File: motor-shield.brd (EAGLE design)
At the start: 65 x 56 mm, 30 parts, among them IC1 24AA01P, K1 PIN20X2

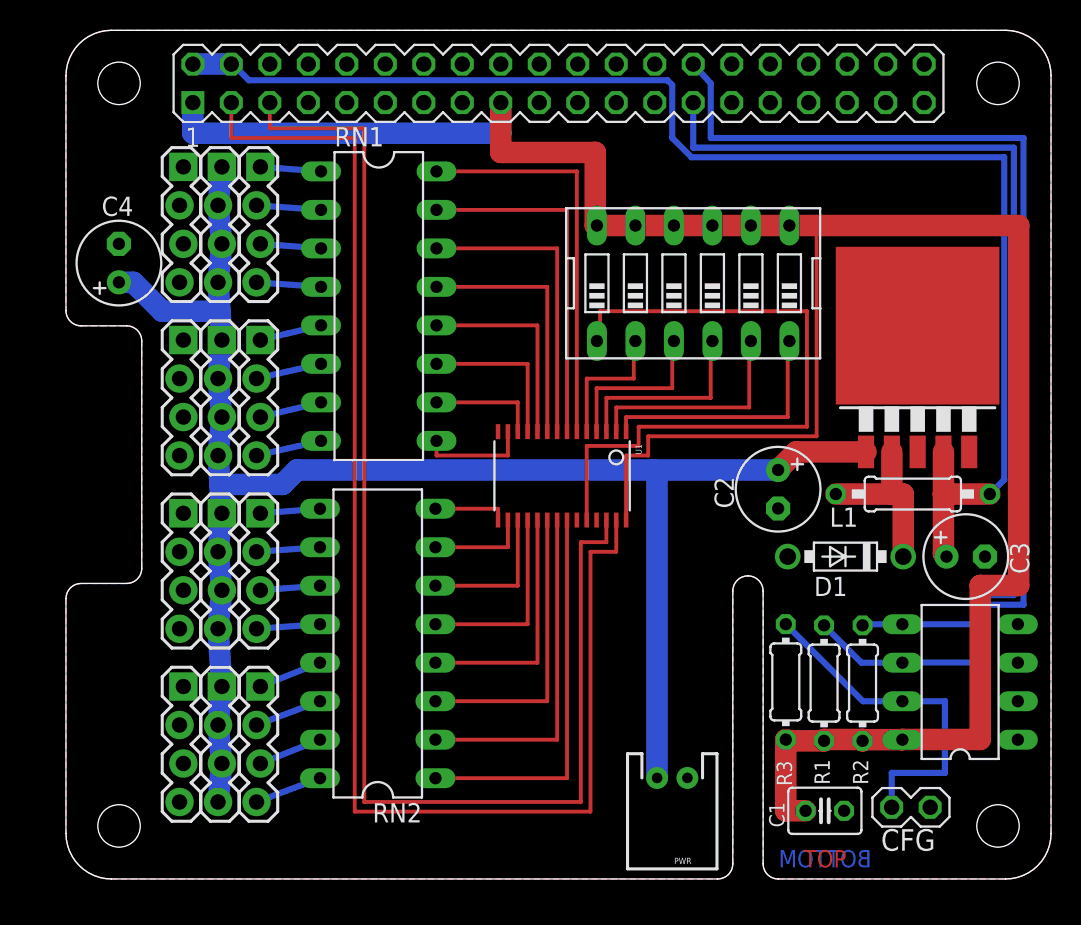
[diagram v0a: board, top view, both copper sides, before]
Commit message: Complete, no air wires, passes DRC
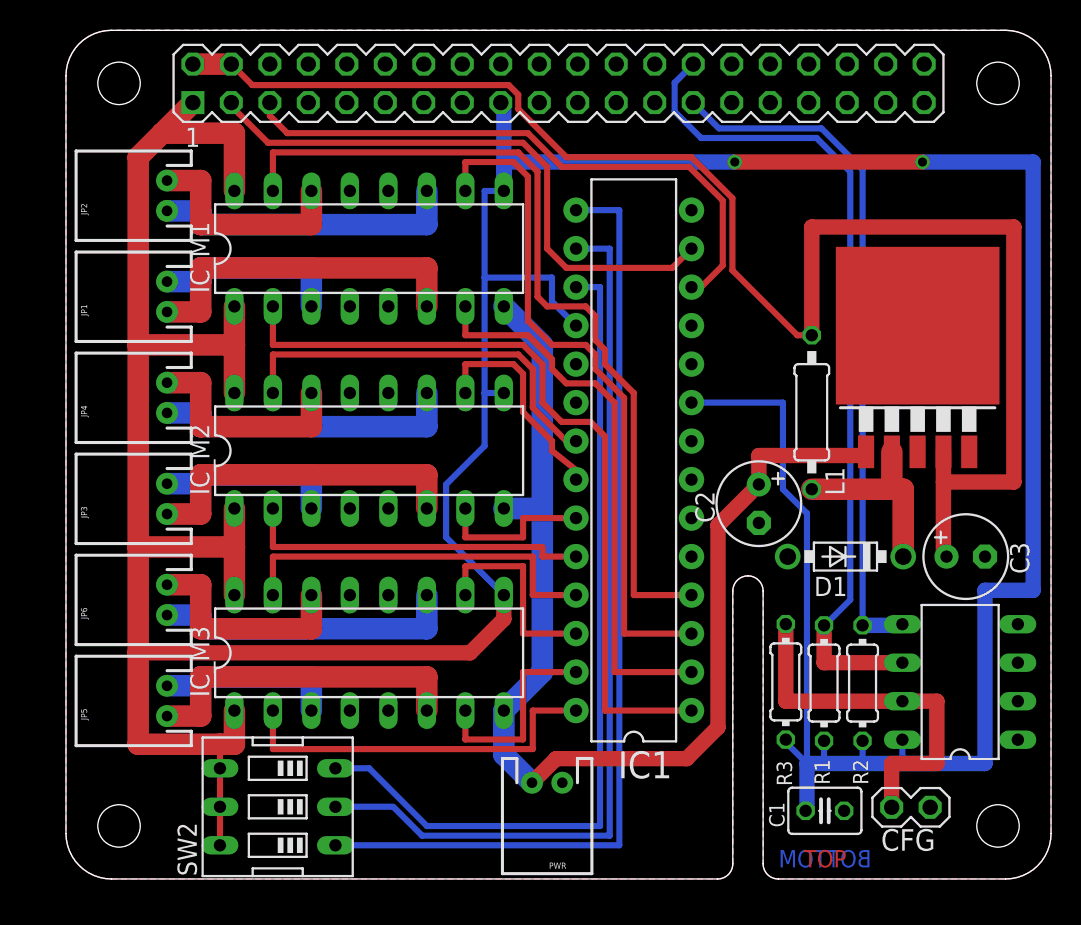
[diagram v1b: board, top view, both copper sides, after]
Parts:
- removed C4: 640uf, rcl:E2,5-6
- removed JP10, JP11, JP12, JP7, JP8, JP9: (no value), SparkFun-Connectors:1X04_LOCK
- removed RN1, RN2: (no value), resistor-dil:DIL16
- removed SW1: (no value), special:EDG-06
- removed U1: (no value), adafruit:TSSOP28
- added IC_ID: 24AA01P, microchip:DIL8
- added IC_M1, IC_M2, IC_M3: L293D, st-microelectronics:DIL16
- added SW2: (no value), special:EDG-03
- IC1: value 24AA01P -> MCP23017SP2; device microchip:DIL8 -> adafruit:DIL28-3-ROUND
- JP1, JP2, JP3, JP4, JP5, JP6: value (none) -> M02JST-PTH-2; device SparkFun-Connectors:1X04_LOCK -> SparkFun-Connectors:JST-2-PTH
- PWR: value (none) -> M02JST-PTH-2
- moved JP5 35.4 mm to (6.67, 11.7), turned to 90 degrees
- moved IC1 26.0 mm to (37.5, 27.6)
- moved JP4 20.0 mm to (6.67, 31.8), turned to 90 degrees
- moved JP6 17.5 mm to (6.67, 18.4), turned to 90 degrees
- moved JP2 11.3 mm to (6.67, 45.1), turned to 90 degrees
- moved JP1 10.5 mm to (6.67, 38.4), turned to 90 degrees
- moved L1 8.58 mm to (49.2, 30.8), turned to 90 degrees
- moved PWR 8.26 mm to (31.8, 6.35)
- moved JP3 6.11 mm to (6.67, 25.1), turned to 90 degrees
- moved C2 1.59 mm to (45.7, 24.8)
- renumbered IC2 to IC_PWR
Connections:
- removed net N$21: JP4.3, RN2.15
- removed net N$22: JP4.4, RN2.16
- removed net N$23: RN2.1, U1.22
- removed net N$24: RN2.2, U1.21
- removed net N$25: RN2.3, U1.20
- removed net N$26: RN2.4, U1.19
- removed net N$27: RN2.5, U1.18
- removed net N$28: RN2.6, U1.17
- removed net N$29: RN1.10, U1.12
- removed net N$30: RN1.11, U1.11
- removed net N$31: RN1.12, U1.10
- removed net N$32: RN1.13, U1.9
- removed net N$33: RN1.14, U1.8
- removed net N$34: RN1.15, U1.7
- removed net N$35: RN1.16, U1.6
- removed net N$36: JP2.1, RN1.5
- removed net N$37: JP2.4, RN1.8
- removed net N$38: JP2.3, RN1.7
- removed net N$39: JP2.2, RN1.6
- new net M1A: IC1.1, IC_M1.2
- new net M1B: IC1.4, IC_M1.15
- new net M2A: IC1.2, IC_M1.7
- new net M2B: IC1.3, IC_M1.10
- new net M3A: IC1.24, IC_M2.2
- new net M3B: IC1.21, IC_M2.15
- new net M4A: IC1.23, IC_M2.7
- new net M4B: IC1.22, IC_M2.10
- new net M5A: IC1.28, IC_M3.2
- new net M5B: IC1.25, IC_M3.15
- new net M6A: IC1.27, IC_M3.7
- new net M6B: IC1.26, IC_M3.10
- net +3V3: now also IC1.18, IC1.9, IC_ID.8, IC_M1.1, IC_M1.16, IC_M1.9, IC_M2.1, IC_M2.16, IC_M2.9, IC_M3.1, IC_M3.16, IC_M3.9, SW2.4, SW2.5, SW2.6; no longer IC1.8, SW1.10, SW1.11, SW1.12, SW1.7, SW1.8, SW1.9, U1.28
- net GND: now also IC1.10, IC_ID.1, IC_ID.2, IC_ID.3, IC_ID.4, IC_M1.12, IC_M1.13, IC_M1.4, IC_M1.5, IC_M2.12, IC_M2.13, IC_M2.4, IC_M2.5, IC_M3.12, IC_M3.13, IC_M3.4, IC_M3.5; no longer C4.-, IC1.1, IC1.2, IC1.3, IC1.4, JP10.1, JP10.2, JP10.3, JP10.4, JP11.1, JP11.2, JP11.3, JP11.4, JP12.1, JP12.2, JP12.3, JP12.4, JP9.1, JP9.2, JP9.3, JP9.4, U1.14, U1.25
- net I2C_SCL: now also IC1.12; no longer U1.26
- net I2C_SDA: now also IC1.13; no longer U1.27
- net ID_SCL: now also IC_ID.6; no longer IC1.6
- net ID_SDA: now also IC_ID.5; no longer IC1.5
- net N$1: now also IC1.17, SW2.3; no longer RN2.7, U1.16
- net N$10: now also IC_M1.3, JP1.2; no longer JP3.2, RN2.10
- net N$11: now also IC_M2.6, JP3.1; no longer SW1.1, U1.24
- net N$12: now also IC_M2.3, JP3.2; no longer SW1.2, U1.5
- net N$13: now also IC_M3.11, JP6.1; no longer SW1.3, U1.4
- net N$14: now also IC_M3.14, JP6.2; no longer SW1.4, U1.3
- net N$15: now also IC_M3.6, JP5.1; no longer SW1.5, U1.2
- net N$16: now also IC_M3.3, JP5.2; no longer SW1.6, U1.1
- net N$17: now also IC1.8; no longer JP3.3, RN2.11
- net N$18: now also IC1.7; no longer JP3.4, RN2.12
- net N$19: now also IC1.6; no longer JP4.1, RN2.13
- net N$2: now also IC1.16, SW2.2; no longer RN2.8, U1.15
- net N$20: now also IC1.5; no longer JP4.2, RN2.14
- net N$3: now also IC1.15, SW2.1; no longer RN1.9, U1.13
- net N$4: now also IC_ID.7; no longer IC1.7
- net N$5: now also IC_M2.11, JP4.1; no longer JP1.4, RN1.4
- net N$6: now also IC_M2.14, JP4.2; no longer JP1.3, RN1.3
- net N$7: now also IC_M1.11, JP2.1; no longer JP1.2, RN1.2
- net N$8: now also IC_M1.14, JP2.2; no longer JP1.1, RN1.1
- net N$9: now also IC_M1.6, JP1.1; no longer JP3.1, RN2.9
- net V+: now also IC_M1.8, IC_M2.8, IC_M3.8; no longer C4.+, JP5.1, JP5.2, JP5.3, JP5.4, JP6.1, JP6.2, JP6.3, JP6.4, JP7.1, JP7.2, JP7.3, JP7.4, JP8.1, JP8.2, JP8.3, JP8.4
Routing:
- net +3V3: track 154.3 -> 296.7 mm, vias 0 -> 2
- net M1B: track 0.00 -> 56.4 mm
- net N$3: track 7.26 -> 63.5 mm
- net N$2: track 4.88 -> 59.8 mm
- net I2C_SDA: track 91.4 -> 38.7 mm
- net M1A: track 0.00 -> 52.2 mm
- net N$1: track 6.57 -> 56.2 mm
- net I2C_SCL: track 87.0 -> 40.0 mm
- net M2B: track 0.00 -> 45.0 mm
- net M2A: track 0.00 -> 36.8 mm
- net V+: track 113.5 -> 77.0 mm
- net N$35: track 26.4 -> 0.00 mm
- net M3B: track 0.00 -> 26.4 mm
- net N$23: track 25.7 -> 0.00 mm
- net M5A: track 0.00 -> 25.1 mm
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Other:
- outline, holes or cut-outs redrawn

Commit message: Rebuilt to match servo shield
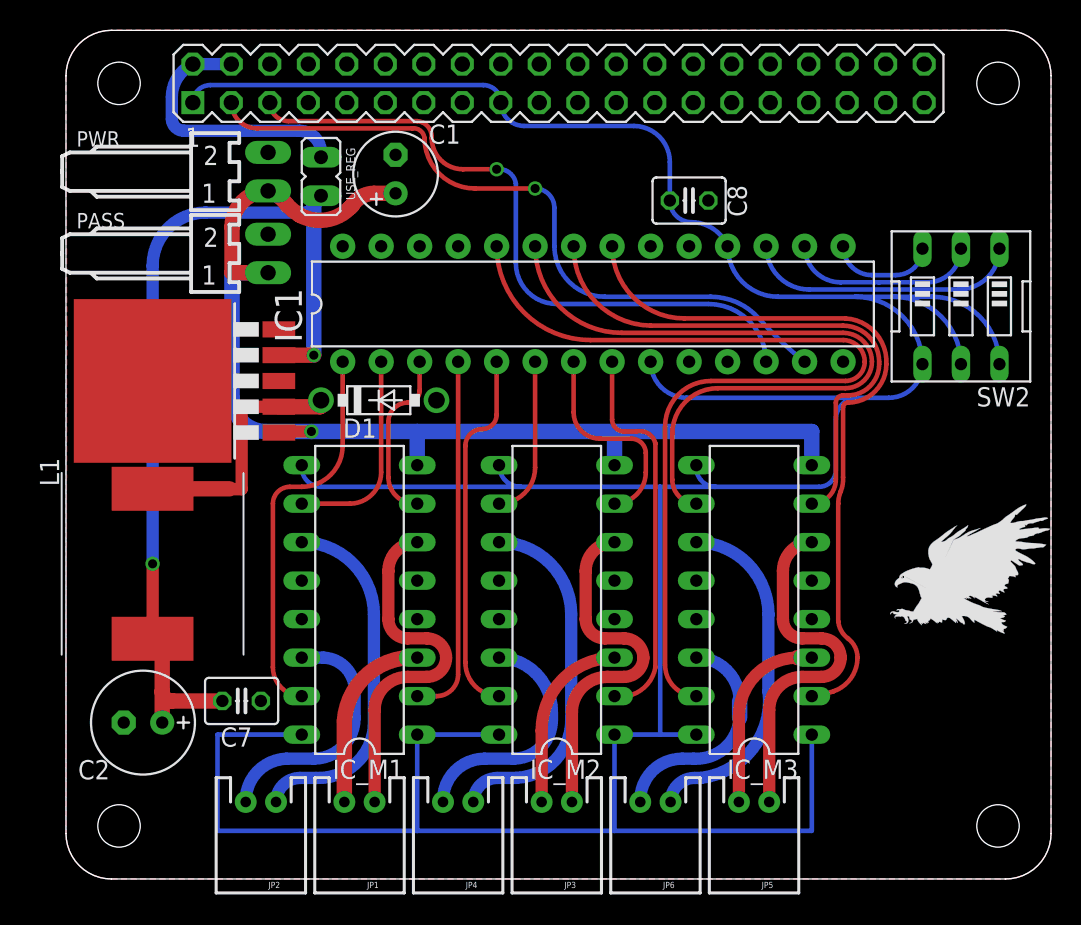
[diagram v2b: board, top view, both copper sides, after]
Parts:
- removed C3: 220uf, rcl:E2,5-6
- removed CFG: (no value), FLYFISH:PIN_W_2
- removed IC_ID: 24AA01P, microchip:DIL8
- removed IC_PWR: (no value), linear:TO263-5
- removed R1, R2: 3k9, rcl:0204/7
- removed R3: 1k, rcl:0204/7
- added C7, C8: 100nf, rcl:C025-030X050
- added IC2: (no value), linear:TO263-5
- added PASS: 22-05-7028-02, con-molex:7395-02
- added U$1: (no value), logo:EAGLE-PLC-8MM
- added USE_REG: (no value), jumper:JP1
- C1: value 100nF -> 1000uf; device rcl:C025-030X050 -> rcl:E2,5-6
- C2: value 680uf -> 1000uf; device rcl:E2,5-6 -> rcl:E2,5-7
- L1: device rcl:0207/10 -> WE-PD:WE-PD_1260/1245/1280/1210
- PWR: value M02JST-PTH-2 -> 22-05-7028-02; device SparkFun-Connectors:JST-2-PTH -> con-molex:7395-02
- moved SW2 55.9 mm to (59.1, 37.8), turned to 180 degrees
- moved C1 50.7 mm to (21.7, 46.5), turned to 90 degrees
- moved L1 44.6 mm to (5.71, 20.8), turned to 270 degrees
- moved PWR 44.3 mm to (13.3, 46.7), turned to 270 degrees
- moved C2 43.1 mm to (5.08, 10.3), turned to 180 degrees
- moved JP2 40.5 mm to (12.9, 5.08), turned to 180 degrees
- moved JP5 39.3 mm to (45.4, 5.08), turned to 180 degrees
- moved JP1 35.7 mm to (19.4, 5.08), turned to 180 degrees
- moved JP6 34.9 mm to (38.9, 5.08), turned to 180 degrees
- moved JP4 32.9 mm to (25.9, 5.08), turned to 180 degrees
- moved JP3 32.6 mm to (32.4, 5.08), turned to 180 degrees
- moved D1 32.5 mm to (20.6, 31.6), turned to 0 degrees
- moved IC_M3 25.6 mm to (45.4, 18.4), turned to 90 degrees
- moved IC_M1 23.2 mm to (19.4, 18.4), turned to 90 degrees
- moved IC_M2 15.8 mm to (32.4, 18.4), turned to 90 degrees
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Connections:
- removed net M1A: IC1.1, IC_M1.2
- removed net M1B: IC1.4, IC_M1.15
- removed net M2A: IC1.2, IC_M1.7
- removed net M2B: IC1.3, IC_M1.10
- removed net M3A: IC1.24, IC_M2.2
- removed net M3B: IC1.21, IC_M2.15
- removed net M4A: IC1.23, IC_M2.7
- removed net M4B: IC1.22, IC_M2.10
- removed net N$1 (its old number): IC1.17, SW2.3
- removed net N$17: IC1.8
- removed net N$18: IC1.7
- removed net N$19: IC1.6
- removed net N$20: IC1.5
- removed net N$3 (its old number): IC1.15, SW2.1
- removed net N$4: CFG.1, IC_ID.7, R3.1
- removed net N$40: D1.C, IC_PWR.2, L1.1
- new net 1F: IC1.4, IC_M1.2
- new net 1R: IC1.3, IC_M1.7
- new net 2F: IC1.1, IC_M1.15
- new net 2R: IC1.2, IC_M1.10
- new net 3F: IC1.8, IC_M2.2
- new net 3R: IC1.7, IC_M2.7
- new net 4F: IC1.5, IC_M2.15
- new net 4R: IC1.6, IC_M2.10
- new net 5F: IC1.21, IC_M3.2
- new net 5R: IC1.22, IC_M3.7
- new net 6F: IC1.24, IC_M3.15
- new net 6R: IC1.23, IC_M3.10
- new net N$16: K1.2, K1.4, USE_REG.2
- new net N$2: IC1.15, SW2.3
- new net N$23: IC1.17, SW2.1
- new net VOUT: D1.C, IC2.2, L1.1
- net +3V3: now also C8.1; no longer C1.1, IC_ID.8, R1.2, R2.2, R3.2
- net +5V: now also C2.+, C7.1, IC2.4, USE_REG.1; no longer C3.+, IC_PWR.4, K1.2, K1.4
- net GND: now also C1.-, C7.2, C8.2, IC2.3, IC2.5, IC2.6, PASS.2, PWR.2; no longer C1.2, C3.-, CFG.2, IC_ID.1, IC_ID.2, IC_ID.3, IC_ID.4, IC_PWR.3, IC_PWR.5, IC_PWR.6, PWR.1
- net ID_SCL: no longer IC_ID.6, R1.1
- net ID_SDA: no longer IC_ID.5, R2.1
- net M5A: no longer IC_M3.2
- net M5B: no longer IC_M3.15
- net M6A: no longer IC_M3.7
- net M6B: no longer IC_M3.10
- net V+: now also C1.+, IC2.1, PASS.1, PWR.1; no longer C2.+, IC_PWR.1, PWR.2
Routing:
- net N$3 (its old number): track 63.5 -> 0.00 mm
- net 6F: track 0.00 -> 61.0 mm
- net +3V3: track 296.7 -> 238.1 mm, vias 2 -> 0
- net M1B: track 56.4 -> 0.00 mm
- net N$1 (its old number): track 56.2 -> 0.00 mm
- net ID_SCL: track 55.2 -> 0.00 mm
- net M1A: track 52.2 -> 0.00 mm
- net N$3: track 59.8 -> 12.2 mm
- net 5F: track 0.00 -> 46.5 mm
- net 6R: track 0.00 -> 45.8 mm
- net ID_SDA: track 45.8 -> 0.00 mm
- net M2B: track 45.0 -> 0.00 mm
- net +5V: track 100.7 -> 60.2 mm, vias 0 -> 2
- net M2A: track 36.8 -> 0.00 mm
- net 5R: track 0.00 -> 34.8 mm
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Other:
- outline, holes or cut-outs redrawn
- board text removed: "BOTTOM"
- board text removed: "TOP"

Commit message: ROTATE THE EAGLE
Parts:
- moved U$1 14.8 mm to (50.5, 3.33), turned to 0 degrees
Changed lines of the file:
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@@
 <attribute name="VALUE" x="10.8951" y="43.2704" size="0.8128" layer="27" ratio="10" rot="R180"/>
 </element>
-<element name="U$1" library="logo" package="EAGLE-PLC-8MM" value="" x="53.6575" y="17.78" rot="R330"/>
+<element name="U$1" library="logo" package="EAGLE-PLC-8MM" value="" x="50.4825" y="3.33375"/>
 <element name="USE_REG" library="jumper" package="JP1" value="" x="16.8275" y="46.355" smashed="yes">
 <attribute name="NAME" x="18.4785" y="48.26" size="0.6096" layer="25" ratio="10" rot="R270"/>
